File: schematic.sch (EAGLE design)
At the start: 126 parts, among them IC1 AD8015, IC2 AD8015, IC3 AD8015, IC4 AD8015

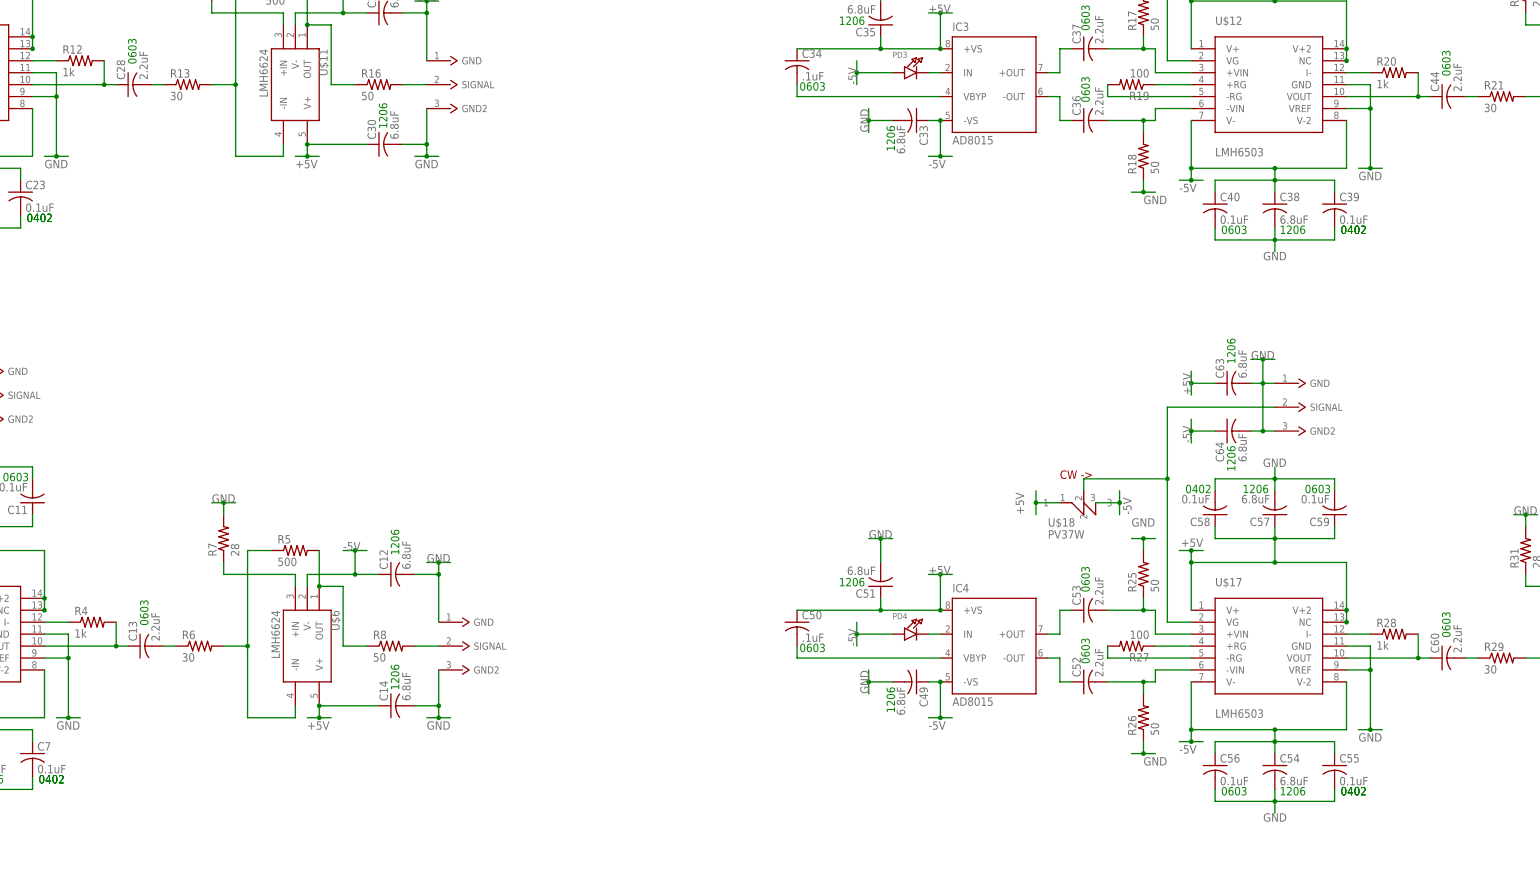
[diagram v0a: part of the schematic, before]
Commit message: Added snubber network to each circuit in schematic and layout
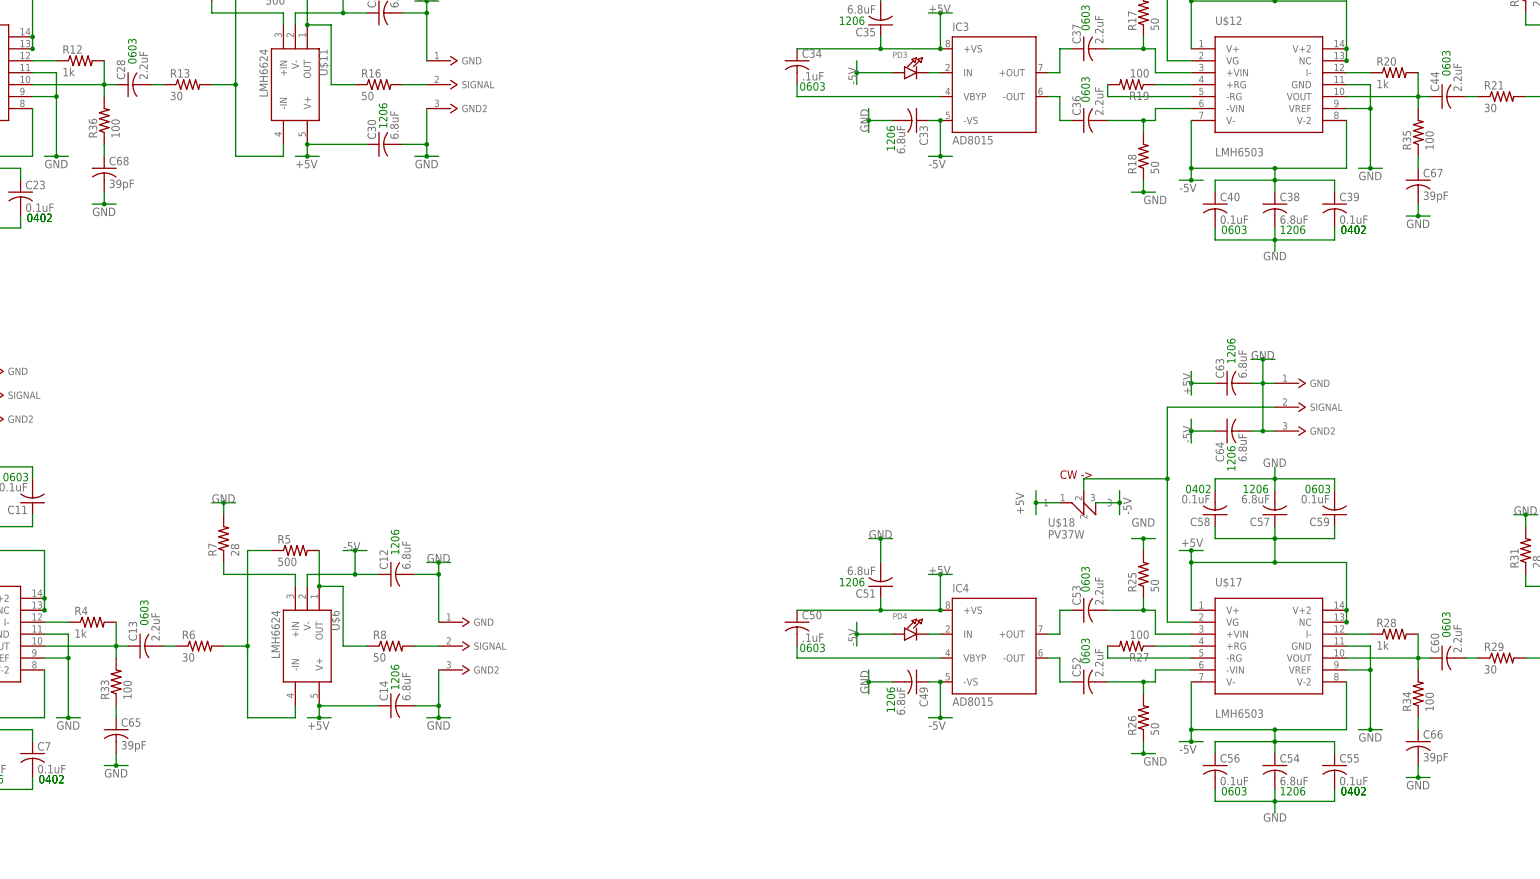
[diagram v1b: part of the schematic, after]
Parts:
- added C65, C66, C67, C68: 39pF, rcl:C-USC0603
- added R33, R34, R35, R36: 100, rcl:R-US_R0603
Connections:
- new net N$91: C65.1, R33.1
- new net N$93: C66.1, R34.1
- new net N$95: C67.1, R35.1
- new net N$97: C68.1, R36.1
- net GND: now also C65.2, C66.2, C67.2, C68.2
- net N$10: now also R33.2
- net N$34: now also R36.2
- net N$56: now also R35.2
- net N$78: now also R34.2
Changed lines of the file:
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@@
 <part name="C64" library="rcl" deviceset="C-US" device="C1206" value="6.8uF"/>
 <part name="U$22" library="12-ChannelEMG" deviceset="DIVERSITYPWR" device=""/>
+<part name="R33" library="rcl" deviceset="R-US_" device="R0603" value="100"/>
+<part name="C65" library="rcl" deviceset="C-US" device="C0603" value="39pF"/>
+<part name="R34" library="rcl" deviceset="R-US_" device="R0603" value="100"/>
+<part name="C66" library="rcl" deviceset="C-US" device="C0603" value="39pF"/>
+<part name="R35" library="rcl" deviceset="R-US_" device="R0603" value="100"/>
+<part name="C67" library="rcl" deviceset="C-US" device="C0603" value="39pF"/>
+<part name="R36" library="rcl" deviceset="R-US_" device="R0603" value="100"/>
+<part name="C68" library="rcl" deviceset="C-US" device="C0603" value="39pF"/>
 </parts>
 <sheets>
@@
 </instance>
 <instance part="U$22" gate="G$1" x="137.16" y="-12.7" rot="R180"/>
+<instance part="R33" gate="G$1" x="147.32" y="43.18" rot="R90"/>
+<instance part="C65" gate="G$1" x="147.32" y="33.02"/>
+<instance part="R34" gate="G$1" x="424.18" y="40.64" rot="R90"/>
+<instance part="C66" gate="G$1" x="424.18" y="30.48"/>
+<instance part="R35" gate="G$1" x="424.18" y="160.02" rot="R90"/>
+<instance part="C67" gate="G$1" x="424.18" y="149.86"/>
+<instance part="R36" gate="G$1" x="144.78" y="162.56" rot="R90"/>
+<instance part="C68" gate="G$1" x="144.78" y="152.4"/>
 </instances>
 <busses>
@@
 <wire x1="142.24" y1="-12.7" x2="144.78" y2="-12.7" width="0.1524" layer="91"/>
 <label x="144.78" y="-12.7" size="1.778" layer="95"/>
+</segment>
+<segment>
+<wire x1="144.78" y1="25.4" x2="147.32" y2="25.4" width="0.1524" layer="91"/>
+<label x="144.78" y="22.86" size="1.778" layer="95"/>
+<pinref part="C65" gate="G$1" pin="2"/>
+<wire x1="147.32" y1="25.4" x2="149.86" y2="25.4" width="0.1524" layer="91"/>
+<wire x1="147.32" y1="25.4" x2="147.32" y2="27.94" width="0.1524" layer="91"/>
+<junction x="147.32" y="25.4"/>
+</segment>
+<segment>
+<wire x1="421.64" y1="22.86" x2="424.18" y2="22.86" width="0.1524" layer="91"/>
+<label x="421.64" y="20.32" size="1.778" layer="95"/>
+<pinref part="C66" gate="G$1" pin="2"/>
+<wire x1="424.18" y1="22.86" x2="426.72" y2="22.86" width="0.1524" layer="91"/>
+<wire x1="424.18" y1="22.86" x2="424.18" y2="25.4" width="0.1524" layer="91"/>
+<junction x="424.18" y="22.86"/>
+</segment>
+<segment>
+<wire x1="421.64" y1="142.24" x2="424.18" y2="142.24" width="0.1524" layer="91"/>
+<label x="421.64" y="139.7" size="1.778" layer="95"/>
+<pinref part="C67" gate="G$1" pin="2"/>
+<wire x1="424.18" y1="142.24" x2="426.72" y2="142.24" width="0.1524" layer="91"/>
+<wire x1="424.18" y1="144.78" x2="424.18" y2="142.24" width="0.1524" layer="91"/>
+<junction x="424.18" y="142.24"/>
+</segment>
+<segment>
+<wire x1="142.24" y1="144.78" x2="144.78" y2="144.78" width="0.1524" layer="91"/>
+<label x="142.24" y="142.24" size="1.778" layer="95"/>
+<pinref part="C68" gate="G$1" pin="2"/>
+<wire x1="144.78" y1="144.78" x2="147.32" y2="144.78" width="0.1524" layer="91"/>
+<wire x1="144.78" y1="144.78" x2="144.78" y2="147.32" width="0.1524" layer="91"/>
+<junction x="144.78" y="144.78"/>
 </segment>
 </net>
@@
 <pinref part="C13" gate="G$1" pin="1"/>
 <wire x1="147.32" y1="50.8" x2="149.86" y2="50.8" width="0.1524" layer="91"/>
+<pinref part="R33" gate="G$1" pin="2"/>
+<wire x1="147.32" y1="48.26" x2="147.32" y2="50.8" width="0.1524" layer="91"/>
 </segment>
 </net>
@@
 <pinref part="C28" gate="G$1" pin="1"/>
 <wire x1="144.78" y1="170.18" x2="147.32" y2="170.18" width="0.1524" layer="91"/>
+<pinref part="R36" gate="G$1" pin="2"/>
+<wire x1="144.78" y1="167.64" x2="144.78" y2="170.18" width="0.1524" layer="91"/>
 </segment>
 </net>
@@
 <pinref part="C44" gate="G$1" pin="1"/>
 <wire x1="424.18" y1="167.64" x2="426.72" y2="167.64" width="0.1524" layer="91"/>
+<pinref part="R35" gate="G$1" pin="2"/>
+<wire x1="424.18" y1="165.1" x2="424.18" y2="167.64" width="0.1524" layer="91"/>
 </segment>
 </net>
@@
 <pinref part="C60" gate="G$1" pin="1"/>
 <wire x1="424.18" y1="48.26" x2="426.72" y2="48.26" width="0.1524" layer="91"/>
+<pinref part="R34" gate="G$1" pin="2"/>
+<wire x1="424.18" y1="45.72" x2="424.18" y2="48.26" width="0.1524" layer="91"/>
 </segment>
 </net>
@@
 </segment>
 </net>
+<net name="N$91" class="0">
+<segment>
+<pinref part="C65" gate="G$1" pin="1"/>
+<pinref part="R33" gate="G$1" pin="1"/>
+<wire x1="147.32" y1="35.56" x2="147.32" y2="38.1" width="0.1524" layer="91"/>
+</segment>
+</net>
+<net name="N$93" class="0">
+<segment>
+<pinref part="C66" gate="G$1" pin="1"/>
+<pinref part="R34" gate="G$1" pin="1"/>
+<wire x1="424.18" y1="33.02" x2="424.18" y2="35.56" width="0.1524" layer="91"/>
+</segment>
+</net>
+<net name="N$95" class="0">
+<segment>
+<pinref part="C67" gate="G$1" pin="1"/>
+<pinref part="R35" gate="G$1" pin="1"/>
+<wire x1="424.18" y1="152.4" x2="424.18" y2="154.94" width="0.1524" layer="91"/>
+</segment>
+</net>
+<net name="N$97" class="0">
+<segment>
+<pinref part="C68" gate="G$1" pin="1"/>
+<pinref part="R36" gate="G$1" pin="1"/>
+<wire x1="144.78" y1="154.94" x2="144.78" y2="157.48" width="0.1524" layer="91"/>
+</segment>
+</net>

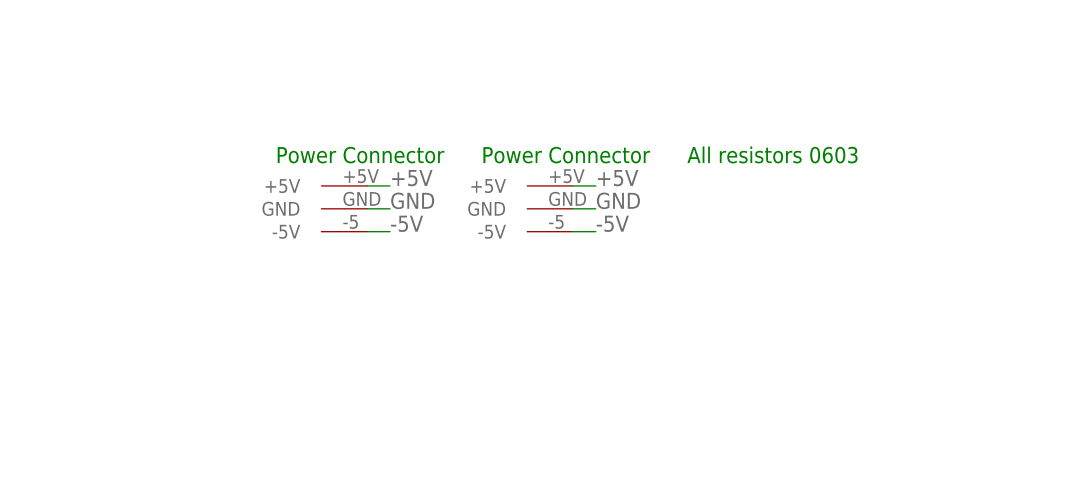
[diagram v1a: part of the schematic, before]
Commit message: Added bypass caps
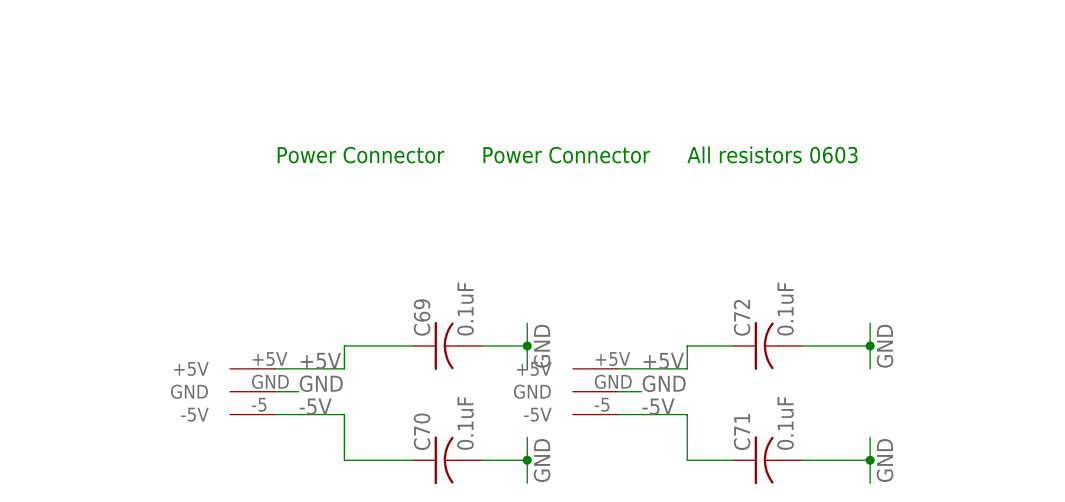
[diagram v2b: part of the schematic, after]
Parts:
- added C69, C70, C71, C72: 0.1uF, rcl:C-USC0402
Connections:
- net +5V: now also C69.1, C72.1
- net -5V: now also C70.1, C71.1
- net GND: now also C69.2, C70.2, C71.2, C72.2
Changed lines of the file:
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@@
 <part name="R36" library="rcl" deviceset="R-US_" device="R0603" value="100"/>
 <part name="C68" library="rcl" deviceset="C-US" device="C0603" value="39pF"/>
+<part name="C69" library="rcl" deviceset="C-US" device="C0402" value="0.1uF"/>
+<part name="C70" library="rcl" deviceset="C-US" device="C0402" value="0.1uF"/>
+<part name="C71" library="rcl" deviceset="C-US" device="C0402" value="0.1uF"/>
+<part name="C72" library="rcl" deviceset="C-US" device="C0402" value="0.1uF"/>
 </parts>
 <sheets>
@@
 <instance part="R6" gate="G$1" x="165.1" y="50.8"/>
 <instance part="U$2" gate="G$1" x="76.2" y="83.82"/>
-<instance part="U$3" gate="G$1" x="114.3" y="-12.7" rot="R180"/>
+<instance part="U$3" gate="G$1" x="104.14" y="-33.02" rot="R180"/>
 <instance part="U$4" gate="G$1" x="116.84" y="104.14"/>
 <instance part="U$5" gate="G$1" x="215.9" y="50.8"/>
@@
 <attribute name="VALUE" x="387.731" y="89.916" size="1.778" layer="96" rot="R90"/>
 </instance>
-<instance part="U$22" gate="G$1" x="137.16" y="-12.7" rot="R180"/>
+<instance part="U$22" gate="G$1" x="142.24" y="-33.02" rot="R180"/>
 <instance part="R33" gate="G$1" x="147.32" y="43.18" rot="R90"/>
 <instance part="C65" gate="G$1" x="147.32" y="33.02"/>
@@
 <instance part="R36" gate="G$1" x="144.78" y="162.56" rot="R90"/>
 <instance part="C68" gate="G$1" x="144.78" y="152.4"/>
+<instance part="C69" gate="G$1" x="127" y="-27.94" rot="R90"/>
+<instance part="C70" gate="G$1" x="127" y="-40.64" rot="R90"/>
+<instance part="C71" gate="G$1" x="162.56" y="-40.64" rot="R90"/>
+<instance part="C72" gate="G$1" x="162.56" y="-27.94" rot="R90"/>
 </instances>
 <busses>
@@
 <segment>
 <pinref part="U$3" gate="G$1" pin="GND"/>
-<wire x1="119.38" y1="-12.7" x2="121.92" y2="-12.7" width="0.1524" layer="91"/>
-<label x="121.92" y="-12.7" size="1.778" layer="95"/>
+<wire x1="109.22" y1="-33.02" x2="111.76" y2="-33.02" width="0.1524" layer="91"/>
+<label x="111.76" y="-33.02" size="1.778" layer="95"/>
 </segment>
 <segment>
@@
 <segment>
 <pinref part="U$22" gate="G$1" pin="GND"/>
-<wire x1="142.24" y1="-12.7" x2="144.78" y2="-12.7" width="0.1524" layer="91"/>
-<label x="144.78" y="-12.7" size="1.778" layer="95"/>
+<wire x1="147.32" y1="-33.02" x2="149.86" y2="-33.02" width="0.1524" layer="91"/>
+<label x="149.86" y="-33.02" size="1.778" layer="95"/>
 </segment>
 <segment>
@@
 <wire x1="144.78" y1="144.78" x2="144.78" y2="147.32" width="0.1524" layer="91"/>
 <junction x="144.78" y="144.78"/>
+</segment>
+<segment>
+<wire x1="175.26" y1="-27.94" x2="175.26" y2="-30.48" width="0.1524" layer="91"/>
+<wire x1="175.26" y1="-27.94" x2="175.26" y2="-25.4" width="0.1524" layer="91"/>
+<label x="177.8" y="-30.48" size="1.778" layer="95" rot="R90"/>
+<junction x="175.26" y="-27.94"/>
+<pinref part="C72" gate="G$1" pin="2"/>
+<wire x1="167.64" y1="-27.94" x2="175.26" y2="-27.94" width="0.1524" layer="91"/>
+</segment>
+<segment>
+<wire x1="175.26" y1="-40.64" x2="175.26" y2="-43.18" width="0.1524" layer="91"/>
+<wire x1="175.26" y1="-40.64" x2="175.26" y2="-38.1" width="0.1524" layer="91"/>
+<label x="177.8" y="-43.18" size="1.778" layer="95" rot="R90"/>
+<junction x="175.26" y="-40.64"/>
+<pinref part="C71" gate="G$1" pin="2"/>
+<wire x1="167.64" y1="-40.64" x2="175.26" y2="-40.64" width="0.1524" layer="91"/>
+</segment>
+<segment>
+<wire x1="137.16" y1="-27.94" x2="137.16" y2="-30.48" width="0.1524" layer="91"/>
+<wire x1="137.16" y1="-27.94" x2="137.16" y2="-25.4" width="0.1524" layer="91"/>
+<label x="139.7" y="-30.48" size="1.778" layer="95" rot="R90"/>
+<junction x="137.16" y="-27.94"/>
+<pinref part="C69" gate="G$1" pin="2"/>
+<wire x1="132.08" y1="-27.94" x2="137.16" y2="-27.94" width="0.1524" layer="91"/>
+</segment>
+<segment>
+<wire x1="137.16" y1="-40.64" x2="137.16" y2="-43.18" width="0.1524" layer="91"/>
+<wire x1="137.16" y1="-40.64" x2="137.16" y2="-38.1" width="0.1524" layer="91"/>
+<label x="139.7" y="-43.18" size="1.778" layer="95" rot="R90"/>
+<junction x="137.16" y="-40.64"/>
+<pinref part="C70" gate="G$1" pin="2"/>
+<wire x1="132.08" y1="-40.64" x2="137.16" y2="-40.64" width="0.1524" layer="91"/>
 </segment>
 </net>
@@
 <segment>
 <pinref part="U$3" gate="G$1" pin="-5V"/>
-<wire x1="119.38" y1="-15.24" x2="121.92" y2="-15.24" width="0.1524" layer="91"/>
-<label x="121.92" y="-15.24" size="1.778" layer="95"/>
+<label x="111.76" y="-35.56" size="1.778" layer="95"/>
+<wire x1="124.46" y1="-40.64" x2="116.84" y2="-40.64" width="0.1524" layer="91"/>
+<wire x1="116.84" y1="-40.64" x2="116.84" y2="-35.56" width="0.1524" layer="91"/>
+<wire x1="116.84" y1="-35.56" x2="109.22" y2="-35.56" width="0.1524" layer="91"/>
+<pinref part="C70" gate="G$1" pin="1"/>
 </segment>
 <segment>
@@
 <segment>
 <pinref part="U$22" gate="G$1" pin="-5V"/>
-<wire x1="142.24" y1="-15.24" x2="144.78" y2="-15.24" width="0.1524" layer="91"/>
-<label x="144.78" y="-15.24" size="1.778" layer="95"/>
+<label x="149.86" y="-35.56" size="1.778" layer="95"/>
+<wire x1="160.02" y1="-40.64" x2="154.94" y2="-40.64" width="0.1524" layer="91"/>
+<wire x1="154.94" y1="-40.64" x2="154.94" y2="-35.56" width="0.1524" layer="91"/>
+<wire x1="154.94" y1="-35.56" x2="147.32" y2="-35.56" width="0.1524" layer="91"/>
+<pinref part="C71" gate="G$1" pin="1"/>
 </segment>
 </net>
@@
 <segment>
 <pinref part="U$3" gate="G$1" pin="+5V"/>
-<wire x1="119.38" y1="-10.16" x2="121.92" y2="-10.16" width="0.1524" layer="91"/>
-<label x="121.92" y="-10.16" size="1.778" layer="95"/>
+<label x="111.76" y="-30.48" size="1.778" layer="95"/>
+<wire x1="124.46" y1="-27.94" x2="116.84" y2="-27.94" width="0.1524" layer="91"/>
+<wire x1="116.84" y1="-27.94" x2="116.84" y2="-30.48" width="0.1524" layer="91"/>
+<wire x1="116.84" y1="-30.48" x2="109.22" y2="-30.48" width="0.1524" layer="91"/>
+<pinref part="C69" gate="G$1" pin="1"/>
 </segment>
 <segment>
@@
 <segment>
 <pinref part="U$22" gate="G$1" pin="+5V"/>
-<wire x1="142.24" y1="-10.16" x2="144.78" y2="-10.16" width="0.1524" layer="91"/>
-<label x="144.78" y="-10.16" size="1.778" layer="95"/>
+<label x="149.86" y="-30.48" size="1.778" layer="95"/>
+<wire x1="160.02" y1="-27.94" x2="154.94" y2="-27.94" width="0.1524" layer="91"/>
+<wire x1="154.94" y1="-27.94" x2="154.94" y2="-30.48" width="0.1524" layer="91"/>
+<wire x1="154.94" y1="-30.48" x2="147.32" y2="-30.48" width="0.1524" layer="91"/>
+<pinref part="C72" gate="G$1" pin="1"/>
 </segment>
 </net>

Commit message: Fixed BNC package and updated schematic labels
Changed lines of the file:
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@@
 <text x="385.318" y="87.884" size="1.778" layer="91" rot="R90">1206</text>
 <text x="132.08" y="-7.62" size="1.778" layer="91">Power Connector</text>
+<text x="158.496" y="33.02" size="1.778" layer="91" rot="R180">0603</text>
+<text x="167.64" y="-21.844" size="1.778" layer="91" rot="R270">0603</text>
+<text x="167.64" y="-34.544" size="1.778" layer="91" rot="R270">0603</text>
+<text x="132.08" y="-34.544" size="1.778" layer="91" rot="R270">0603</text>
+<text x="132.08" y="-21.844" size="1.778" layer="91" rot="R270">0603</text>
 </plain>
 <instances>
